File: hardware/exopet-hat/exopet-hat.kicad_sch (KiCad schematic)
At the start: 51 parts, among them J1 12V DC in, J10 CH3 12V OUT, J11 CH4 dry contact, J13 FLOAT1 switch, J14 FLOAT2 switch, J3 RPi GPIO (HAT), J4 TEMP (3V3/DATA/GND), J8 CH1 12V OUT, J9 CH2 12V OUT, K1 G5LE-1-CF DC12, K2 G5LE-1-CF DC12, K3 G5LE-1-CF DC12, K4 G5LE-1-CF DC12, Q1 AOD403, U2 TBD62003AFG, U4 CAT24C32, U5 5V ESD clamp (SOD-323)

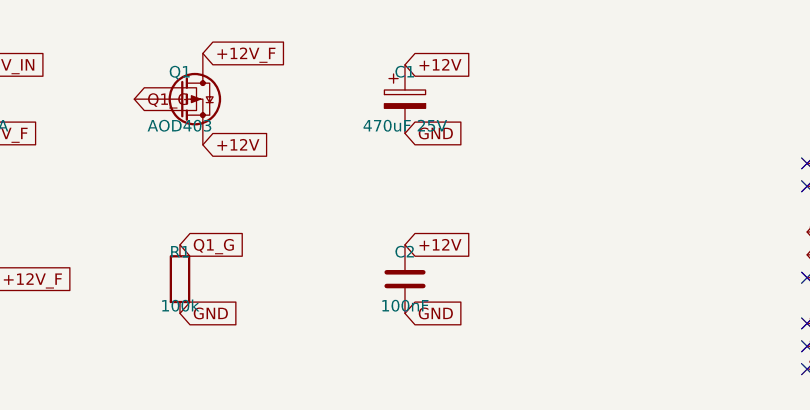
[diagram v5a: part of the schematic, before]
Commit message: Fix GPIO socket to bottom side per official HAT template; refresh fab package
Critical fix caught before ordering: the 2x20 socket body was generated
on the top side and off-position — physically unable to mate with a Pi.
Now matches KiCad's official RaspberryPi-HAT template exactly (B.Cu,
pin 1 at 8.37,4.77 from the hole datum) with tools/verify_j3.py as a
permanent regression assert.

Also: C1 changed to low-profile 6.3x7.7mm (330uF) for under-HAT
clearance; verified in-stock LCSC codes baked into the assembly BOM
(PC104 stacking socket C35165, CUI PJ-102A C20518877, KF350 terminals,
RGEF500/RXEF110 fuses, PESD5V0S1BA ESD diode, 1x5 socket C50950).
Rerouted, DRC clean (0 errors), renders and fab files regenerated.

Co-Authored-By: Claude Fable 5 <noreply@anthropic.com>
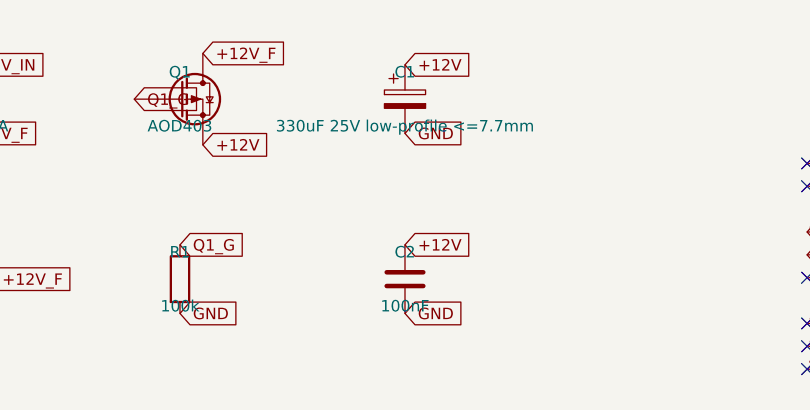
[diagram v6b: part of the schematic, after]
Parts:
- C1: value 470uF 25V -> 330uF 25V low-profile <=7.7mm; footprint Capacitor_THT:CP_Radial_D8.0mm_P3.50mm -> Capacitor_SMD:CP_Elec_6.3x7.7
- U5: LCSC VERIFY -> C19224
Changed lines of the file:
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@@
     (exclude_from_sim no) (in_bom yes) (on_board yes) (dnp no)
     (property "Reference" "C1" (at 105 37 0) (effects (font (size 1.27 1.27))))
-    (property "Value" "470uF 25V" (at 105 43 0) (effects (font (size 1.27 1.27))))
-    (property "Footprint" "Capacitor_THT:CP_Radial_D8.0mm_P3.50mm" (at 105 40 0) (effects (font (size 1.27 1.27)) hide))
+    (property "Value" "330uF 25V low-profile <=7.7mm" (at 105 43 0) (effects (font (size 1.27 1.27))))
+    (property "Footprint" "Capacitor_SMD:CP_Elec_6.3x7.7" (at 105 40 0) (effects (font (size 1.27 1.27)) hide))
     (property "LCSC" "VERIFY" (at 105 40 0) (effects (font (size 1.27 1.27)) hide))
     (pin "1")
@@
     (property "Value" "5V ESD clamp (SOD-323)" (at 60 158 0) (effects (font (size 1.27 1.27))))
     (property "Footprint" "Diode_SMD:D_SOD-323" (at 60 155 0) (effects (font (size 1.27 1.27)) hide))
-    (property "LCSC" "VERIFY" (at 60 155 0) (effects (font (size 1.27 1.27)) hide))
-    (pin "1")
-    (pin "2")
+    (property "LCSC" "C19224" (at 60 155 0) (effects (font (size 1.27 1.27)) hide))
+    (pin "1")
+    (pin "2")

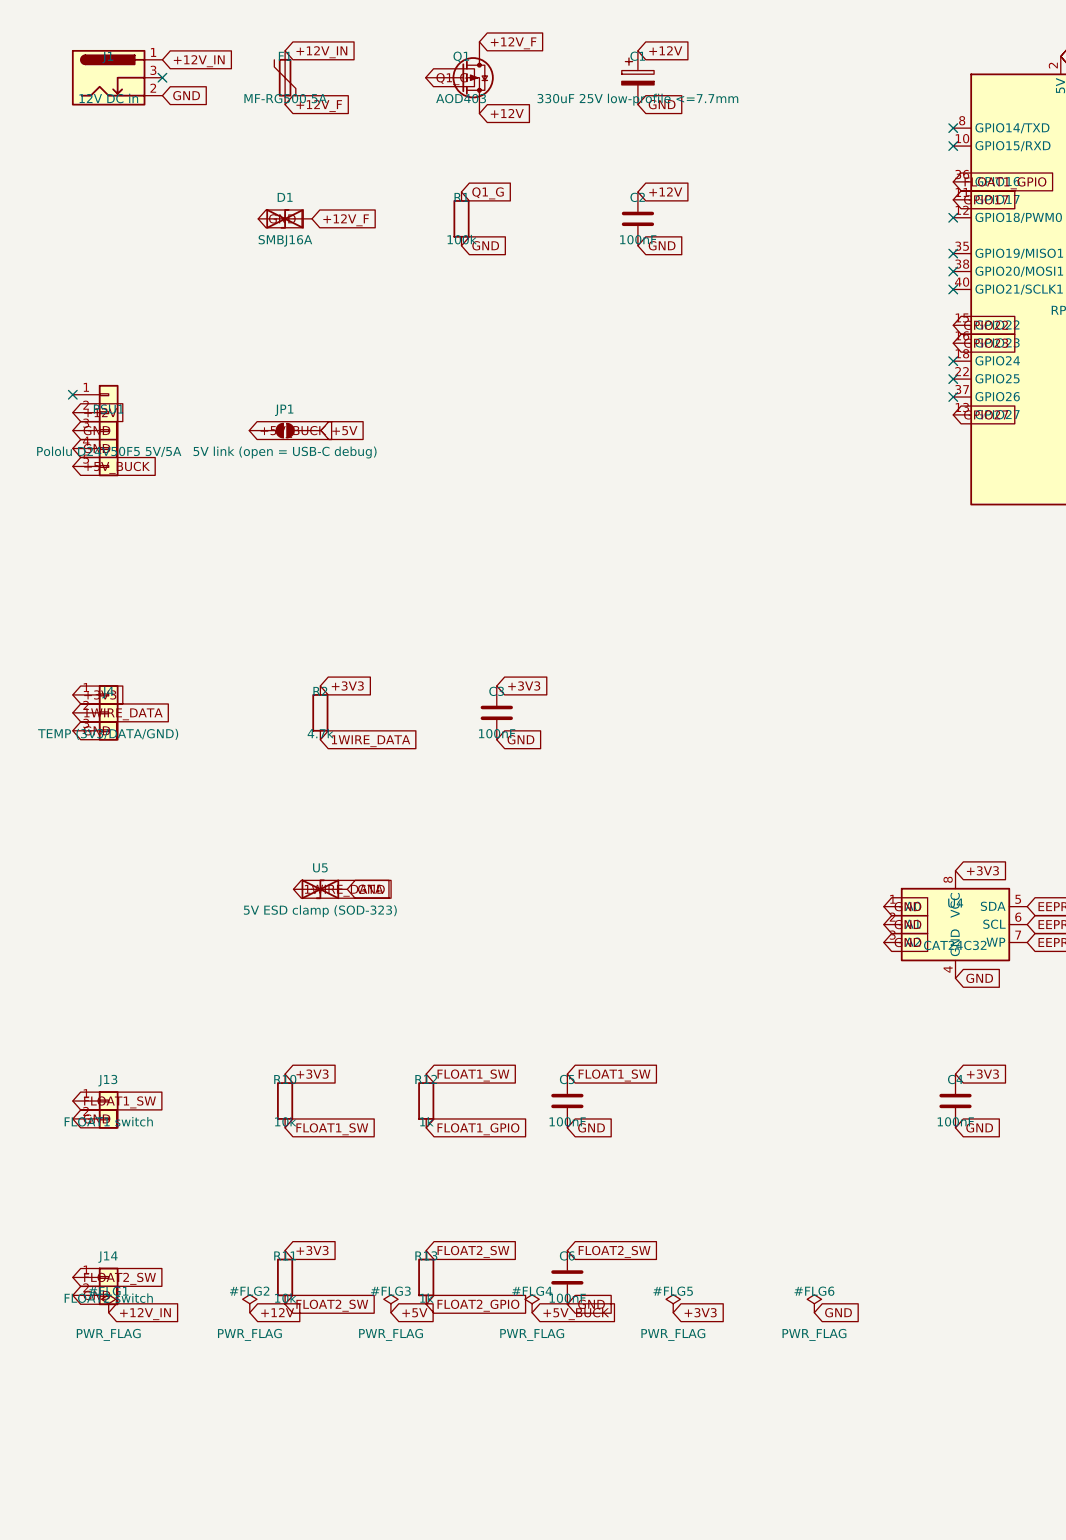
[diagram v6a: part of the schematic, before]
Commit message: HAT rev 2: schematic + placement — integrated buck, D1 fix, top LEDs, TPs
TPS54302 synchronous buck replaces the Pololu socket (datasheet-derived
5.06V design; 5A TPS54531 didn't fit the relay-pad corridors). D1 nets
corrected + bidirectional SMBJ16CA. Channel LEDs move to the top
between terminal blocks; 12V/5V rail LEDs + 4 test points top-left.
Terminal +/- and COM/NO/NC silk, jack polarity text, PTC fuse drills
enlarged to 1.1mm. New check_polarity.py lints every polarized part
from the netlist; check_placement.py now also catches SMD-vs-THT-pad
collisions (found two latent rev-1 near-misses). ERC clean, polarity
lint clean, placement clean, J3 template-verified.

Co-Authored-By: Claude Fable 5 <noreply@anthropic.com>
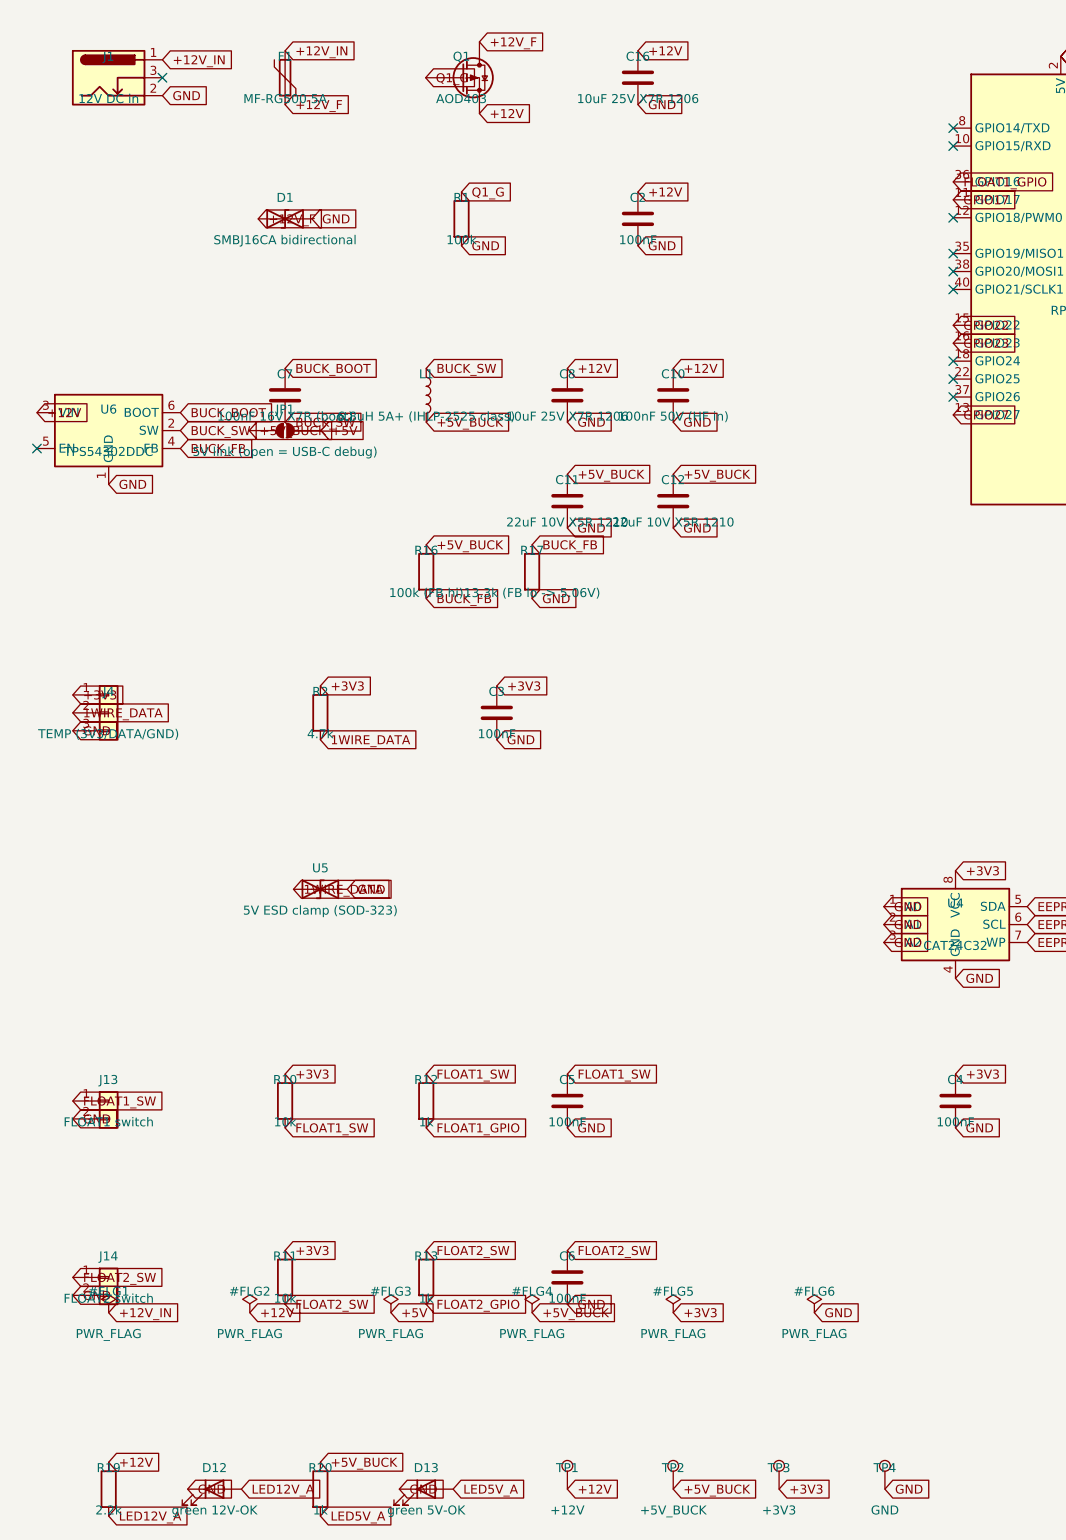
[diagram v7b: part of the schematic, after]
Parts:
- removed C1: 330uF 25V low-profile <=7.7mm, Capacitor_SMD:CP_Elec_6.3x7.7, symbol Device:C_Polarized
- removed PSU1: Pololu D24V50F5 5V/5A, Connector_PinSocket_2.54mm:PinSocket_1x05_P2.54mm_Vertical, symbol Connector_Generic:Conn_01x05
- added C10: 100nF 50V (HF in), Capacitor_SMD:C_0805_2012Metric, symbol Device:C
- added C11, C12: 22uF 10V X5R 1210, Capacitor_SMD:C_1210_3225Metric, symbol Device:C
- added C16, C8: 10uF 25V X7R 1206, Capacitor_SMD:C_1206_3216Metric, symbol Device:C
- added C7: 100nF 16V X7R (boot), Capacitor_SMD:C_0805_2012Metric, symbol Device:C
- added D12: green 12V-OK, LED_SMD:LED_0805_2012Metric, symbol Device:LED
- added D13: green 5V-OK, LED_SMD:LED_0805_2012Metric, symbol Device:LED
- added L1: 6.8uH 5A+ (IHLP-2525 class), Inductor_SMD:L_Vishay_IHLP-2525, symbol Device:L
- added R16: 100k (FB hi), Resistor_SMD:R_0805_2012Metric, symbol Device:R
- added R17: 13.3k (FB lo -> 5.06V), Resistor_SMD:R_0805_2012Metric, symbol Device:R
- added R19: 2.2k, Resistor_SMD:R_0805_2012Metric, symbol Device:R
- added R20: 1k, Resistor_SMD:R_0805_2012Metric, symbol Device:R
- added TP1: +12V, TestPoint:TestPoint_Pad_D1.5mm, symbol Connector:TestPoint
- added TP2: +5V_BUCK, TestPoint:TestPoint_Pad_D1.5mm, symbol Connector:TestPoint
- added TP3: +3V3, TestPoint:TestPoint_Pad_D1.5mm, symbol Connector:TestPoint
- added TP4: GND, TestPoint:TestPoint_Pad_D1.5mm, symbol Connector:TestPoint
- added U6: TPS54302DDC, Package_TO_SOT_SMD:SOT-23-6, symbol Regulator_Switching:TPS54302
- D1: value SMBJ16A -> SMBJ16CA bidirectional
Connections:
- net +12V: now also C10.1, C16.1, C8.1, R19.1, TP1.1, U6.3 (VIN)
- net +12V_F: now also D1.1 (A1); no longer D1.2 (A2)
- net +3V3: now also TP3.1
- net +5V_BUCK: now also C11.1, C12.1, L1.2, R16.1, R20.1, TP2.1
- net GND: now also D1.2 (A2), C10.2, C11.2, C12.2, C16.2, C8.2, D12.1 (K), D13.1 (K), R17.2, TP4.1, U6.1 (GND); no longer D1.1 (A1)
- new net BUCK_BOOT: C7.1, U6.6 (BOOT)
- new net BUCK_FB: R16.2, R17.1, U6.4 (FB)
- new net BUCK_SW: C7.2, L1.1, U6.2 (SW)
- new net LED12V_A: D12.2 (A), R19.2
- new net LED5V_A: D13.2 (A), R20.2

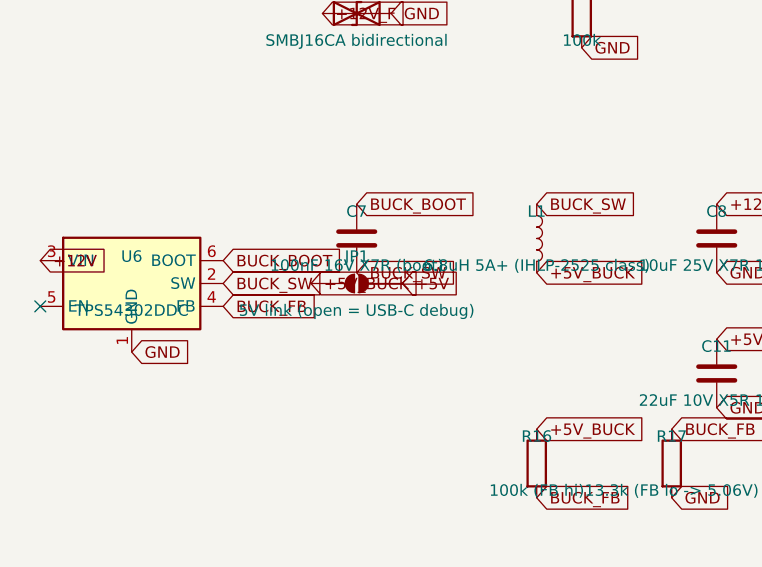
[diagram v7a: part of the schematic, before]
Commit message: HAT rev 2: production-ready 5V link, visible title, deterministic routing
- JP1 hand-soldered jumper replaced by machine-placed 0R (R21): boards
  leave assembly fully powered, no per-board hand step for inventory;
  remove with an iron to isolate the buck for debug.
- 'ExoPet HAT rev2' title moved from under the relays to the top-edge
  strip where it stays visible assembled.
- Route pipeline de-lotteried: DSN exports with the board edge inset
  0.2mm in memory (kills copper-to-edge shaves) and the locked +3V3
  pre-route extends through the EEPROM cluster (C4->R3->R4), which the
  router stranded on varying seeds. Preflight fully green: DRC 0/0,
  golden 208-pin audit, fab cross-check (62 refs). Mockups refreshed.

Co-Authored-By: Claude Fable 5 <noreply@anthropic.com>
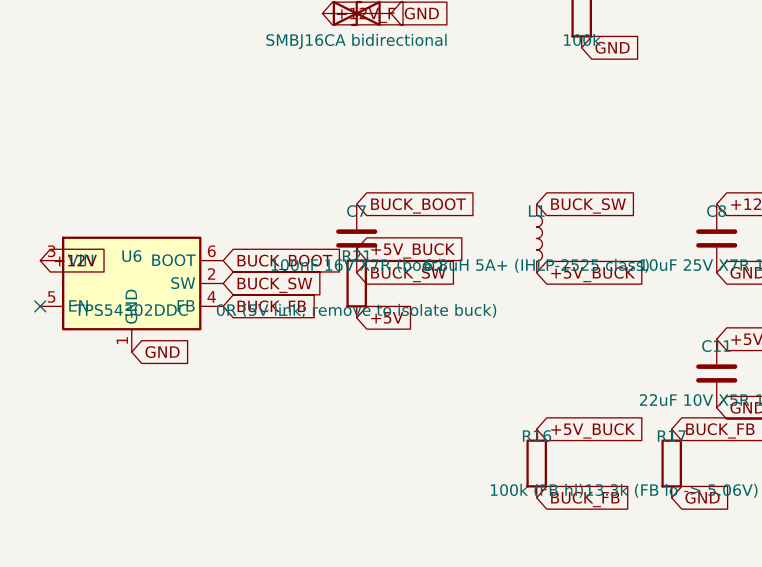
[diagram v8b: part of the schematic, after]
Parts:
- removed JP1: 5V link (open = USB-C debug), Jumper:SolderJumper-2_P1.3mm_Open_RoundedPad1.0x1.5mm, symbol Jumper:SolderJumper_2_Open
- added R21: 0R (5V link; remove to isolate buck), Resistor_SMD:R_0805_2012Metric, symbol Device:R
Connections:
- net +5V: now also R21.2
- net +5V_BUCK: now also R21.1
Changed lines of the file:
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@@
     )
   )
-  (symbol (lib_id "Jumper:SolderJumper_2_Open") (at 55 90 0) (unit 1)
-    (exclude_from_sim no) (in_bom yes) (on_board yes) (dnp no)
-    (property "Reference" "JP1" (at 55 87 0) (effects (font (size 1.27 1.27))))
-    (property "Value" "5V link (open = USB-C debug)" (at 55 93 0) (effects (font (size 1.27 1.27))))
-    (property "Footprint" "Jumper:SolderJumper-2_P1.3mm_Open_RoundedPad1.0x1.5mm" (at 55 90 0) (effects (font (size 1.27 1.27)) hide))
-    (property "LCSC" "" (at 55 90 0) (effects (font (size 1.27 1.27)) hide))
-    (pin "1")
-    (pin "2")
-    (instances
-      (project "exopet-hat"
-        (path "/e0a7e100-0000-4000-8000-00000000c0de" (reference "JP1") (unit 1))
+  (symbol (lib_id "Device:R") (at 55 90 0) (unit 1)
+    (exclude_from_sim no) (in_bom yes) (on_board yes) (dnp no)
+    (property "Reference" "R21" (at 55 87 0) (effects (font (size 1.27 1.27))))
+    (property "Value" "0R (5V link; remove to isolate buck)" (at 55 93 0) (effects (font (size 1.27 1.27))))
+    (property "Footprint" "Resistor_SMD:R_0805_2012Metric" (at 55 90 0) (effects (font (size 1.27 1.27)) hide))
+    (property "LCSC" "C17477" (at 55 90 0) (effects (font (size 1.27 1.27)) hide))
+    (pin "1")
+    (pin "2")
+    (instances
+      (project "exopet-hat"
+        (path "/e0a7e100-0000-4000-8000-00000000c0de" (reference "R21") (unit 1))
       )
     )
@@
   (global_label "+3V3" (shape input) (at 125.0 240.0 0) (effects (font (size 1.27 1.27)) (justify left)))
   (global_label "GND" (shape input) (at 140.0 240.0 0) (effects (font (size 1.27 1.27)) (justify left)))
-  (global_label "+5V_BUCK" (shape input) (at 49.92 90.0 0) (effects (font (size 1.27 1.27)) (justify left)))
-  (global_label "+5V" (shape input) (at 60.08 90.0 0) (effects (font (size 1.27 1.27)) (justify left)))
+  (global_label "+5V_BUCK" (shape input) (at 55.0 86.19 0) (effects (font (size 1.27 1.27)) (justify left)))
+  (global_label "+5V" (shape input) (at 55.0 93.81 0) (effects (font (size 1.27 1.27)) (justify left)))
   (global_label "+3V3" (shape input) (at 175.08 36.98 0) (effects (font (size 1.27 1.27)) (justify left)))
   (global_label "+3V3" (shape input) (at 175.08 36.98 0) (effects (font (size 1.27 1.27)) (justify left)))
